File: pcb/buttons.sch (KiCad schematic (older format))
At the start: 75 parts

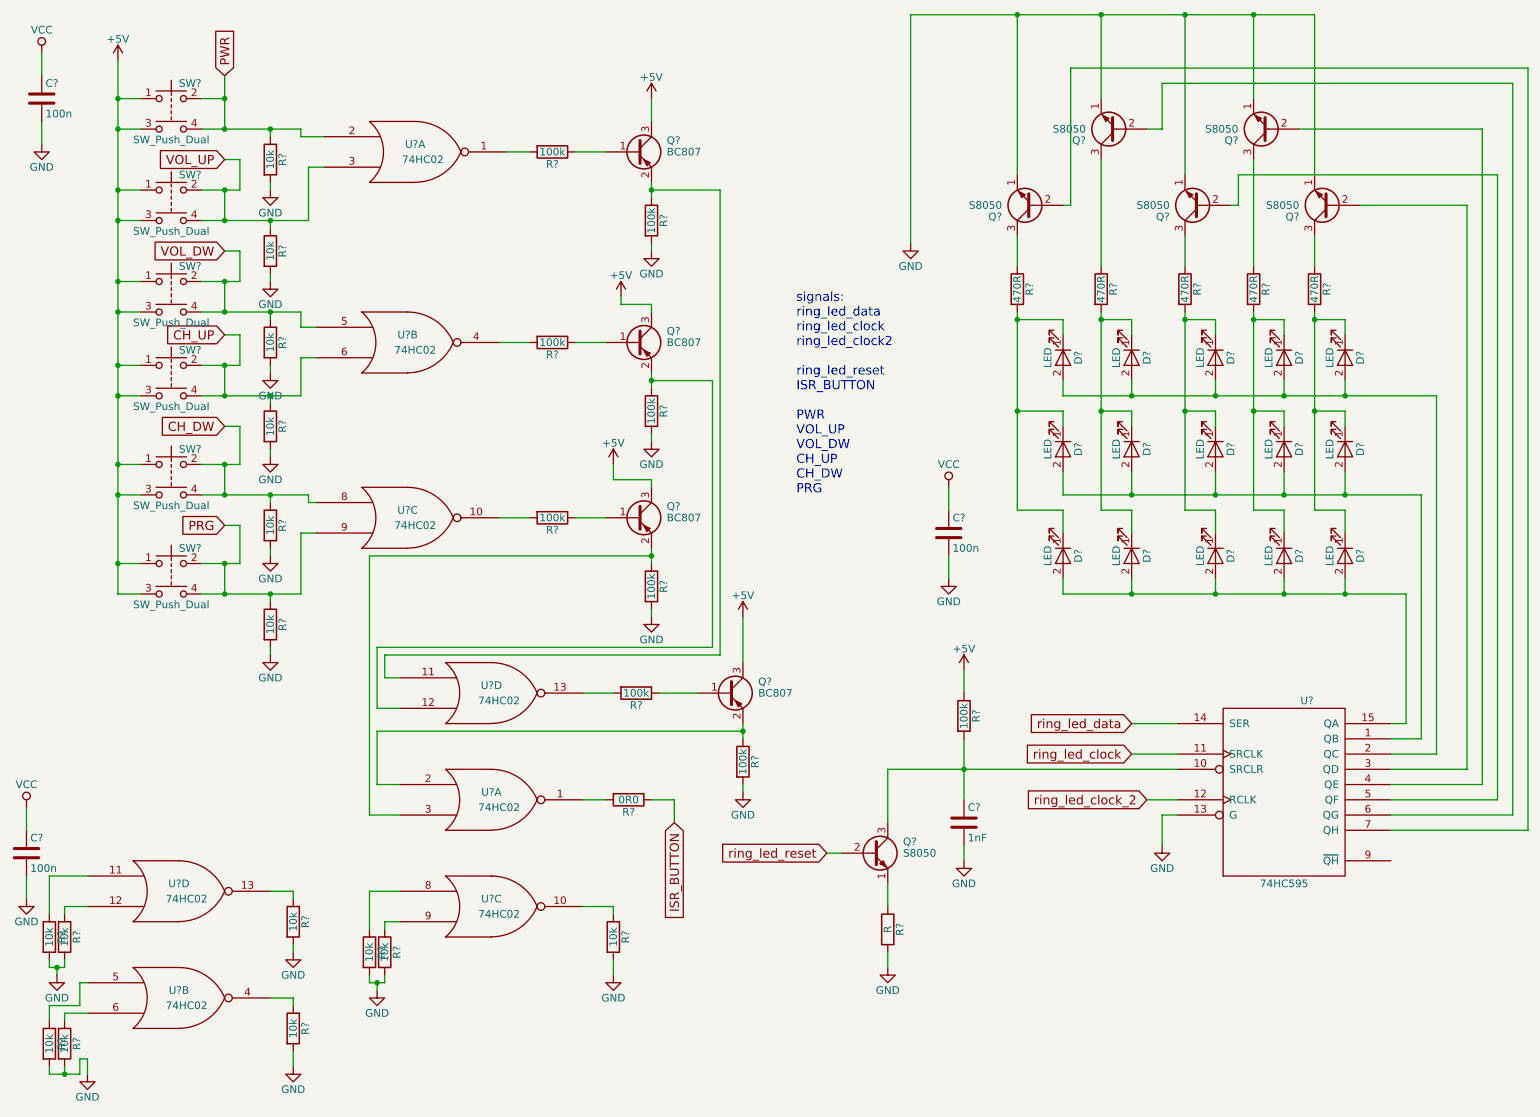
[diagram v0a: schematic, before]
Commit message: nightly | pcb build, routing, placing
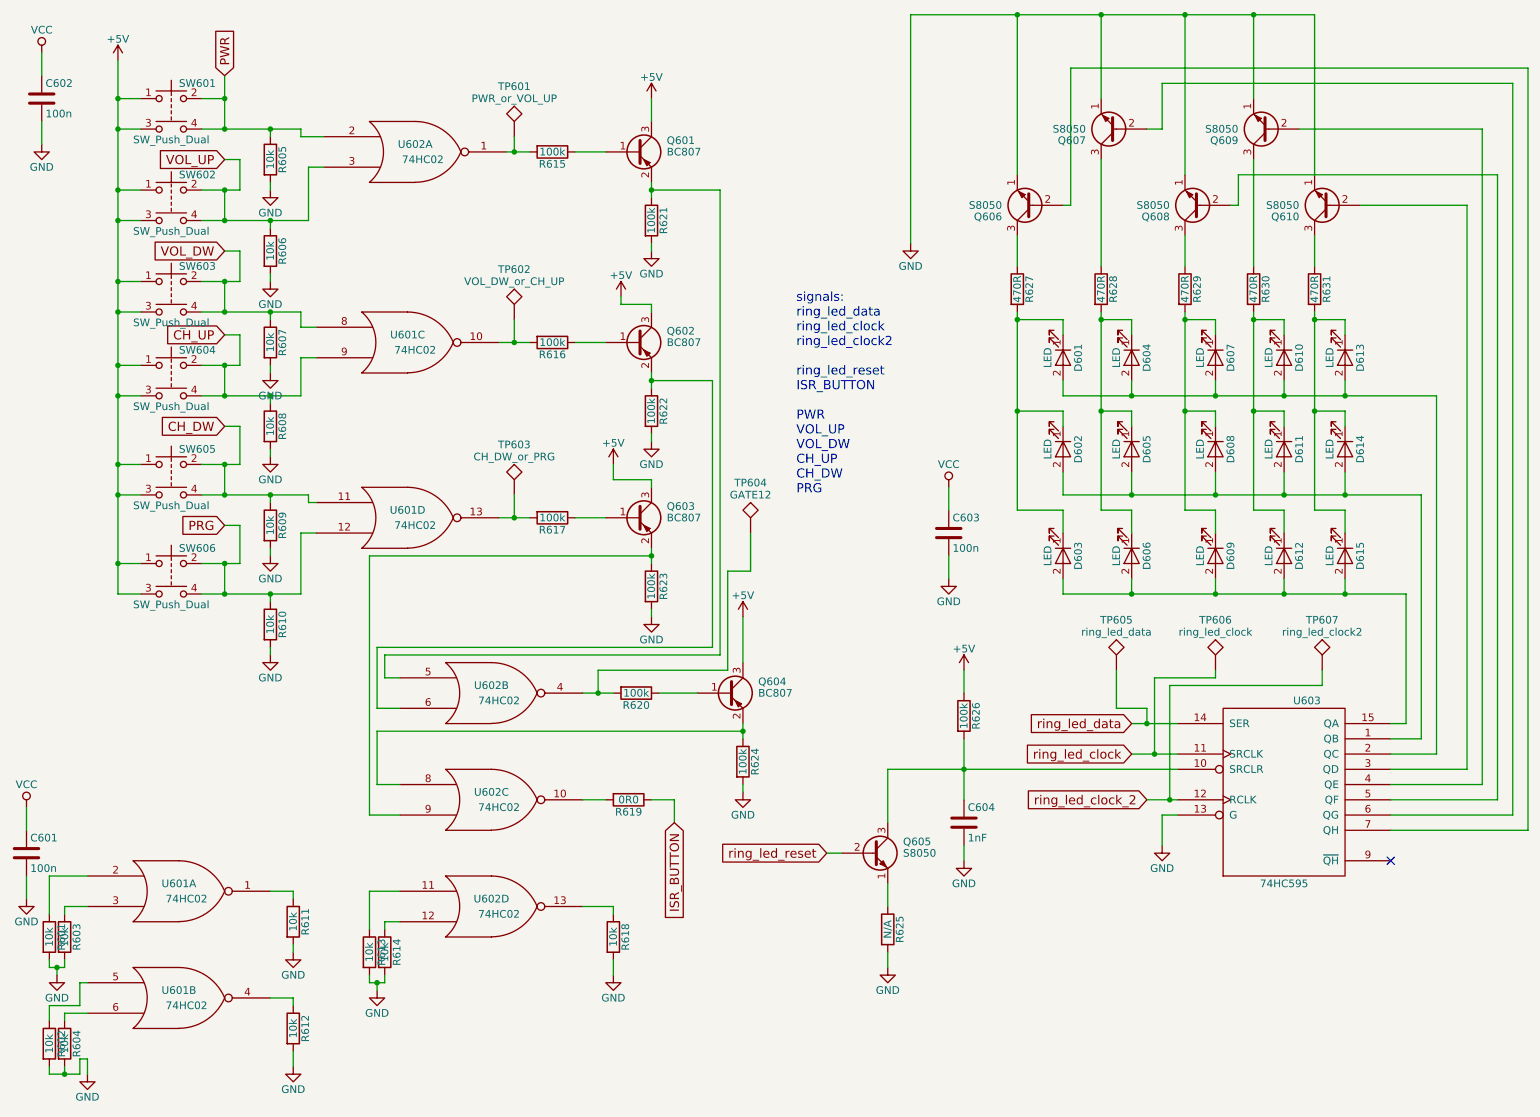
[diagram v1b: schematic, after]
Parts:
- added TP601: PWR_or_VOL_UP, Measurement_Points:Measurement_Point_Round-SMD-Pad_Big, symbol TEST
- added TP602: VOL_DW_or_CH_UP, Measurement_Points:Measurement_Point_Round-SMD-Pad_Big, symbol TEST
- added TP603: CH_DW_or_PRG, Measurement_Points:Measurement_Point_Round-SMD-Pad_Big, symbol TEST
- added TP604: GATE12, Measurement_Points:Measurement_Point_Round-SMD-Pad_Big, symbol TEST
- added TP605: ring_led_data, Measurement_Points:Measurement_Point_Round-SMD-Pad_Big, symbol TEST
- added TP606: ring_led_clock, Measurement_Points:Measurement_Point_Round-SMD-Pad_Big, symbol TEST
- added TP607: ring_led_clock2, Measurement_Points:Measurement_Point_Round-SMD-Pad_Big, symbol TEST
- C601: renamed from C?; footprint (none) -> Capacitors_SMD:C_0603_HandSoldering
- C602, C603, C604: renamed from C?; footprint (none) -> Capacitors_SMD:C_0603
- D601, D602, D603, D604, D605, D606, D607, D608, D609, D610, D611, D612, D613, D614, D615: renamed from D?; footprint (none) -> Resistors_SMD:R_0603_HandSoldering
- Q601, Q602, Q603, Q604: renamed from Q?; footprint TO_SOT_Packages_SMD:SOT-23 -> TO_SOT_Packages_SMD:SOT-23_Handsoldering
- Q605, Q606, Q607, Q608, Q609, Q610: renamed from Q?; footprint TO_SOT_Packages_THT:TO-92_Molded_Narrow -> TO_SOT_Packages_SMD:SOT-23_Handsoldering
- R601, R602, R603, R604, R605, R606, R607, R608, R609, R610, R611, R612, R613, R614, R615, R616, R617, R618, R619, R620, R621, R622, R623, R624, R626, R627, R628, R629, R630, R631: renamed from R?; footprint (none) -> Resistors_SMD:R_0603_HandSoldering
- R625: renamed from R?; value R -> N/A; footprint (none) -> Resistors_SMD:R_0603_HandSoldering
- SW601, SW602, SW603, SW604, SW605, SW606: renamed from SW?; footprint (none) -> Buttons_Switches_THT:SW_TH_Tactile_Omron_B3F-10xx
- U601, U602: renamed from U?; footprint (none) -> Housings_SSOP:TSSOP-14_4.4x5mm_Pitch0.65mm
- U603: renamed from U?; footprint (none) -> Housings_SSOP:TSSOP-16_4.4x5mm_Pitch0.65mm
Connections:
- net CH_DW: now also U601.11; no longer U601.8
- net CH_UP: now also U601.9; no longer U601.6
- net PRG: now also U601.12; no longer U601.9
- net VOL_DW: now also U601.8; no longer U601.5
- net ring_led_clock: now also TP606.1
- net ring_led_clock_2: now also TP607.1
- net ring_led_data: now also TP605.1
- net at R615.2, U602.1: now also TP601.1
- net at R616.2: now also U601.10, TP602.1; no longer U601.4
- net at R617.2: now also U601.13, TP603.1; no longer U601.10
- net at Q601.2 (E), R621.1: now also U602.5; no longer U602.11
- net at Q602.2 (E), R622.1: now also U602.6; no longer U602.12
- net at R620.2: now also U602.4, TP604.1; no longer U602.13
- net at R619.2: now also U602.10; no longer U602.1
- net at Q604.2 (E), R624.1: now also U602.8; no longer U602.2
- net at Q603.2 (E), R623.1: now also U602.9; no longer U602.3
- net at R618.1: now also U602.13; no longer U602.10
- net at R613.1: now also U602.11; no longer U602.8
- net at R614.1: now also U602.12; no longer U602.9
- net at R601.1: now also U601.2; no longer U601.11
- net at R603.1: now also U601.3; no longer U601.12
- net at R611.1: now also U601.1; no longer U601.13
- no-connect marks 0 -> 1
